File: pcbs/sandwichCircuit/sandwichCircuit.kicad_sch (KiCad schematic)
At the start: 1 part, among them U1 ESP32-DevKitC

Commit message: Progress sandwhich board
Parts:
- added IC1: 3678, 3678, symbol SamacSys_Parts:3678
- added J1: NodeMCU aux header, Connector_PinHeader_2.54mm:PinHeader_1x19_P2.54mm_Vertical, symbol Connector:Conn_01x19_Pin
- added J2: North Connector, Connector_PinSocket_2.54mm:PinSocket_1x06_P2.54mm_Vertical, symbol Connector_Generic:Conn_01x06
- added J3: East Connector, Connector_PinSocket_2.54mm:PinSocket_1x06_P2.54mm_Vertical, symbol Connector_Generic:Conn_01x06
- added J4: West Connector, Connector_PinSocket_2.54mm:PinSocket_1x06_P2.54mm_Vertical, symbol Connector_Generic:Conn_01x06
- added J5: Audio Out, Connector_PinHeader_2.54mm:PinHeader_1x03_P2.54mm_Vertical, symbol Connector_Generic:Conn_01x03
- U1: value ESP32-DevKitC -> ESP32-DevKitC header; footprint 113990105 -> Espressif:ESP32-DevKitC
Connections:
- net +3.3V: now reaches U1.1 (3V3)
- net +3.3V: now also IC1.2 (3VD), J2.5 (Pin_5)
- net BCLK: now reaches U1.10 (DAC_2/ADC2_CH9/GPIO26)
- net BCLK: now also IC1.6 (BCLK)
- net GND: now reaches U1.14 (GND), U1.32 (GND), U1.38 (GND)
- net GND: now also IC1.3 (GND), J1.1 (Pin_1), J1.7 (Pin_7), J2.1 (Pin_1)
- net +5V: now reaches U1.19 (5V)
- net +5V: now also IC1.1 (VIN), J2.4 (Pin_4)
- net CLK: now reaches U1.20 (SD_CLK/GPIO6)
- net CLK: now also J1.19 (Pin_19)
- net D0: now reaches U1.21 (SD_DATA0/GPIO7)
- net D0: now also J1.18 (Pin_18)
- net D1: now reaches U1.22 (SD_DATA1/GPIO8)
- net D1: now also J1.17 (Pin_17)
- net GPIO15: now reaches U1.23 (MTDO/GPIO15/ADC2_CH3)
- net GPIO15: now also J1.16 (Pin_16)
- net GPIO2: now reaches U1.24 (ADC2_CH2/GPIO2)
- net GPIO2: now also J1.15 (Pin_15)
- net GPIO0: now reaches U1.25 (GPIO0/BOOT/ADC2_CH1)
- net GPIO0: now also J1.14 (Pin_14)
- net GPIO4: now reaches U1.26 (ADC2_CH0/GPIO4)
- net GPIO4: now also J1.13 (Pin_13)
- net GPIO16/U1RXD: now reaches U1.27 (GPIO16)
- net GPIO16/U1RXD: now also J1.12 (Pin_12)
- net GPIO17/U1TXD: now reaches U1.28 (GPIO17)
- net GPIO17/U1TXD: now also J1.11 (Pin_11)
- net GPIO5: now reaches U1.29 (GPIO5)
- net GPIO5: now also J1.10 (Pin_10)
- net GPIO18: now reaches U1.30 (GPIO18)
- net GPIO18: now also J1.9 (Pin_9)
- net GPIO19: now reaches U1.31 (GPIO19)
- net GPIO19: now also J1.8 (Pin_8)
- net GPIO21: now reaches U1.33 (GPIO21)
- net GPIO21: now also J1.6 (Pin_6)
- net GPIO3/U0RXD: now reaches U1.34 (U0RXD/GPIO3)
- net GPIO3/U0RXD: now also J1.5 (Pin_5)
- net GPIO1/U0TXD: now reaches U1.35 (U0TXD/GPIO1)
- net GPIO1/U0TXD: now also J1.4 (Pin_4)
- net DIN: now reaches U1.36 (GPIO22)
- net DIN: now also IC1.5 (DIN), J1.3 (Pin_3)
- net GPIO23: now reaches U1.37 (GPIO23)
- net GPIO23: now also J1.2 (Pin_2)
- net WSEL: now reaches U1.9 (DAC_1/ADC2_CH8/GPIO25)
- net WSEL: now also IC1.4 (WSEL)
- new net AGND: IC1.8 (AGND), J5.1 (Pin_1)
- new net CTS: J4.2 (Pin_2)
- new net DCD: J4.5 (Pin_5)
- new net DSR: J4.4 (Pin_4)
- new net DTR: J2.6 (Pin_6)
- new net IO0: J3.5 (Pin_5)
- new net IO1: J3.4 (Pin_4)
- new net IO2: J3.3 (Pin_3)
- new net IO3: J3.2 (Pin_2)
- new net LOUT: IC1.7 (LOUT), J5.3 (Pin_3)
- new net RI: J4.6 (Pin_6)
- new net ROUT: IC1.9 (ROUT), J5.2 (Pin_2)
- new net RST: J3.1 (Pin_1)
- new net RTS: J4.3 (Pin_3)
- new net RXD: J2.2 (Pin_2)
- new net SPD: J4.1 (Pin_1)
- new net SPD-: J3.6 (Pin_6)
- new net TXD: J2.3 (Pin_3)
- no-connect marks 0 -> 24

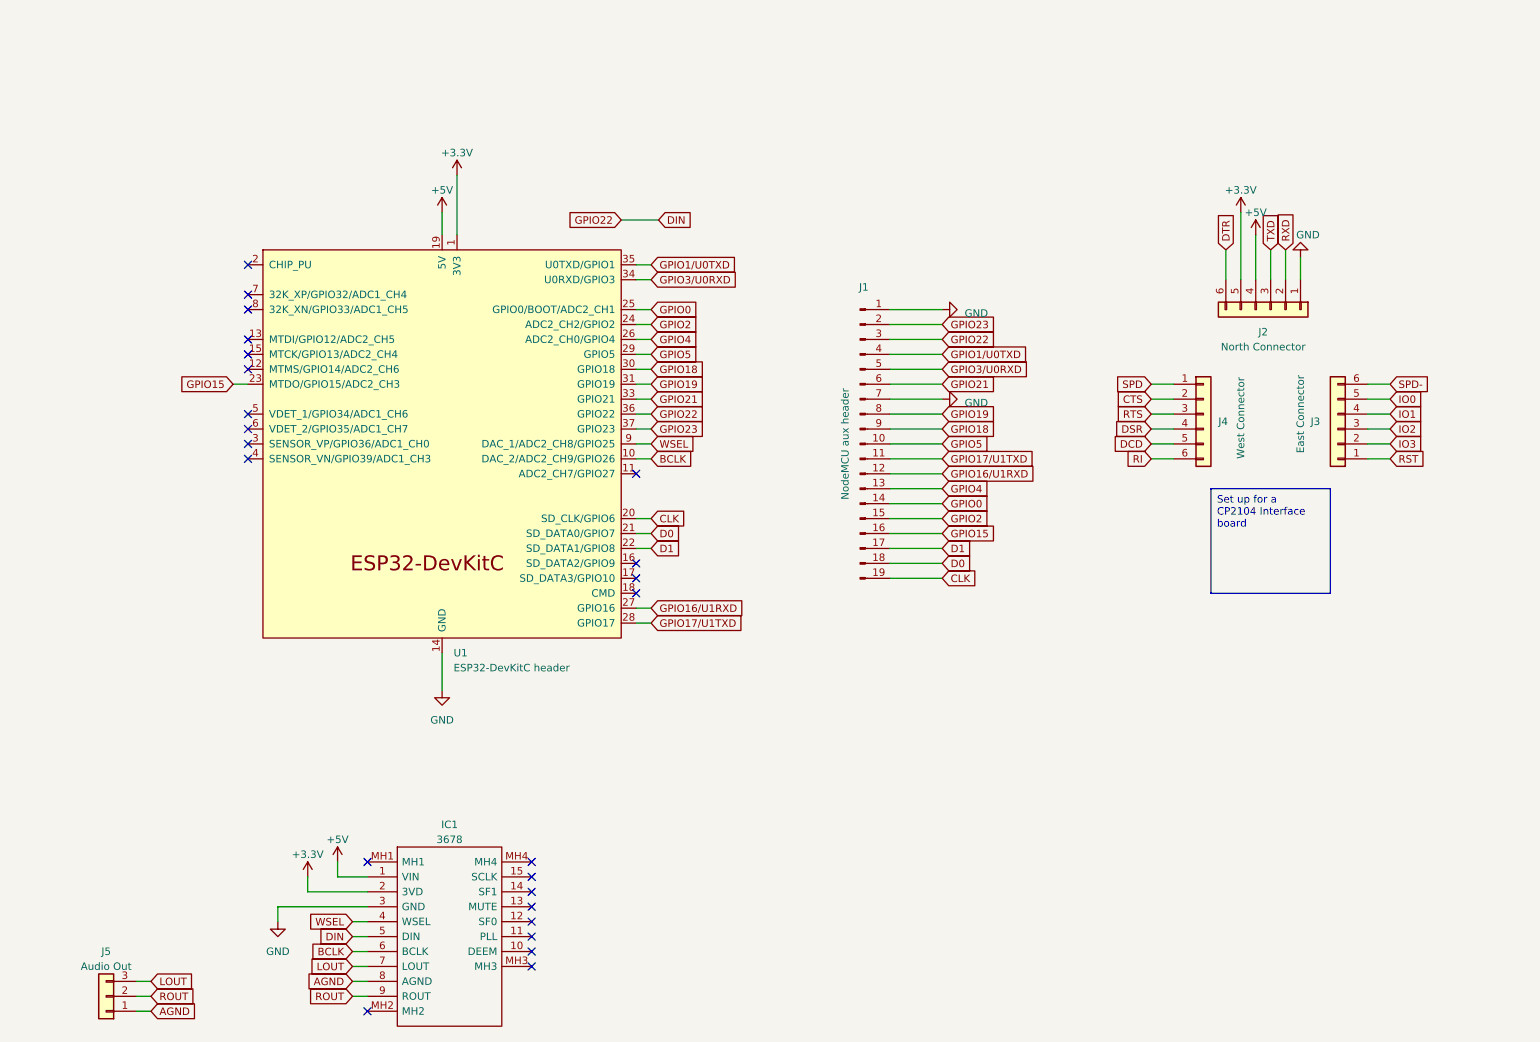
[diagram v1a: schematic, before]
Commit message: Simplified footprints, schematic revisited
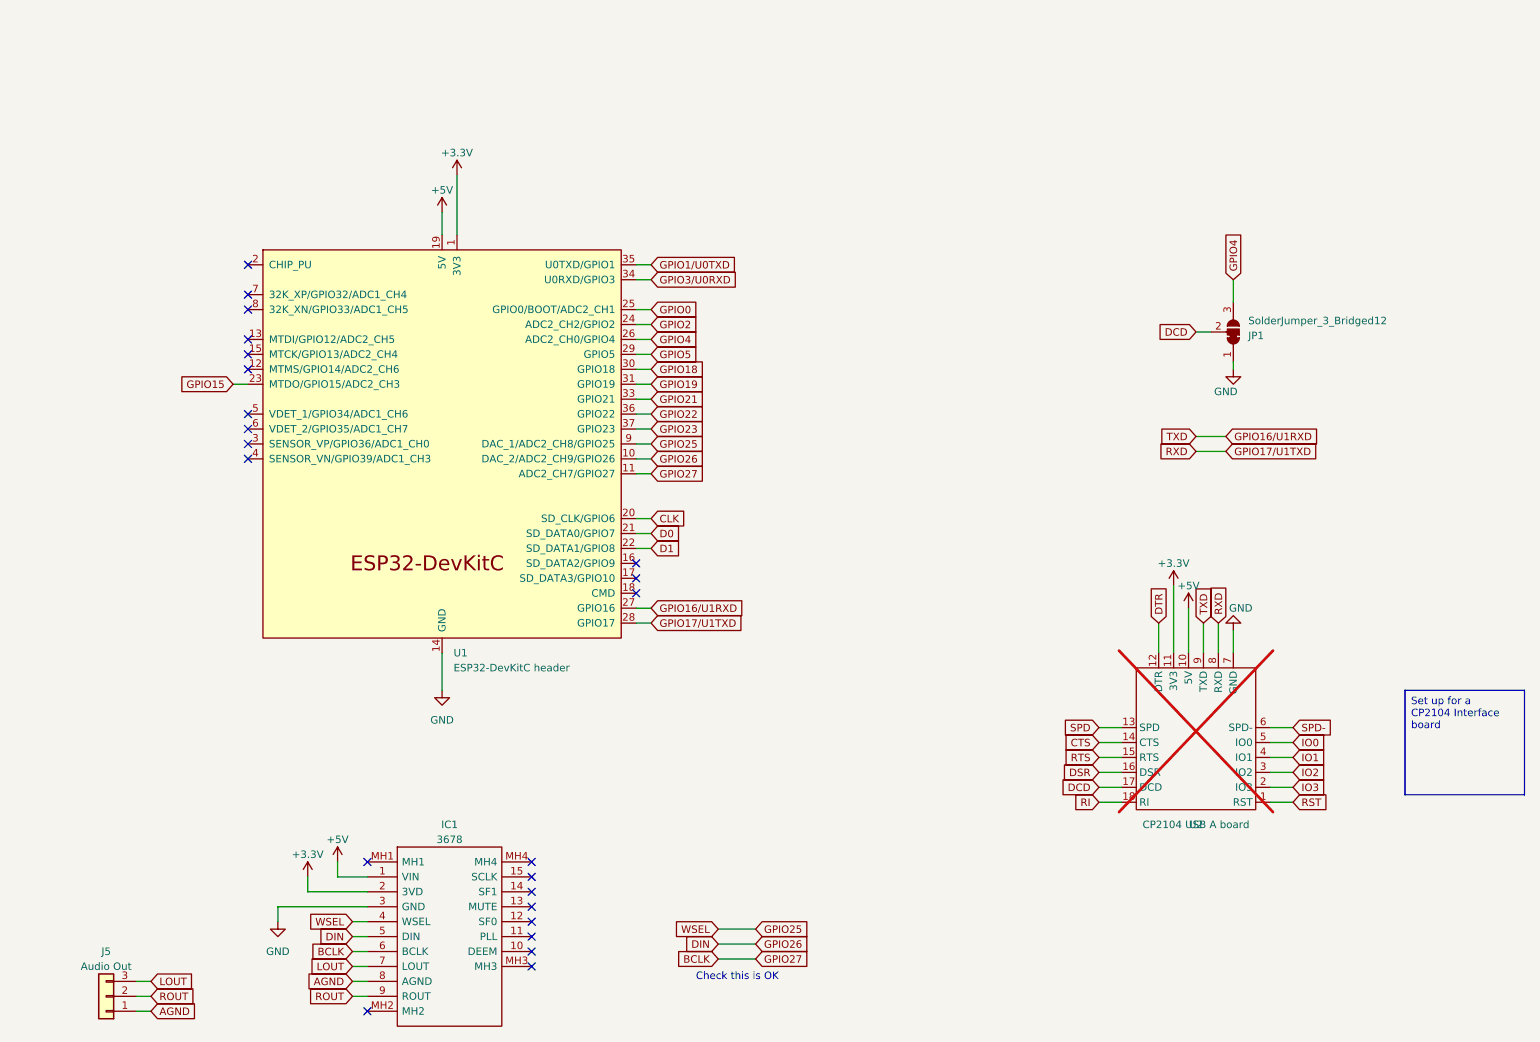
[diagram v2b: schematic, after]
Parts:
- removed J1: NodeMCU aux header, Connector_PinHeader_2.54mm:PinHeader_1x19_P2.54mm_Vertical, symbol Connector:Conn_01x19_Pin
- removed J2: North Connector, Connector_PinSocket_2.54mm:PinSocket_1x06_P2.54mm_Vertical, symbol Connector_Generic:Conn_01x06
- removed J3: East Connector, Connector_PinSocket_2.54mm:PinSocket_1x06_P2.54mm_Vertical, symbol Connector_Generic:Conn_01x06
- removed J4: West Connector, Connector_PinSocket_2.54mm:PinSocket_1x06_P2.54mm_Vertical, symbol Connector_Generic:Conn_01x06
- added JP1: SolderJumper_3_Bridged12, Jumper:SolderJumper-3_P1.3mm_Bridged12_RoundedPad1.0x1.5mm, symbol Jumper:SolderJumper_3_Bridged12
- added U2: CP2104 USB A board, DIY:CP2104_USB_Board, symbol DIY:CP2104_UART_Board
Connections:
- net +3.3V: now also U2.11 (3V3)
- net +5V: now also U2.10 (5V)
- net BCLK: now also U1.11 (ADC2_CH7/GPIO27); no longer U1.10 (DAC_2/ADC2_CH9/GPIO26)
- net CTS: now also U2.14 (CTS)
- net DCD: now also JP1.2 (C), U2.17 (DCD)
- net DIN: now also U1.10 (DAC_2/ADC2_CH9/GPIO26); no longer U1.36 (GPIO22)
- net DSR: now also U2.16 (DSR)
- net DTR: now also U2.12 (DTR)
- net GND: now also JP1.1 (A), U2.7 (GND)
- net GPIO16/U1RXD: now also U2.9 (TXD)
- net GPIO17/U1TXD: now also U2.8 (RXD)
- net GPIO4: now also JP1.3 (B)
- net IO0: now also U2.5 (IO0)
- net IO1: now also U2.4 (IO1)
- net IO2: now also U2.3 (IO2)
- net IO3: now also U2.2 (IO3)
- net RI: now also U2.18 (RI)
- net RST: now also U2.1 (RST)
- net RTS: now also U2.15 (RTS)
- net SPD: now also U2.13 (SPD)
- net SPD-: now also U2.6 (SPD-)
- net WSEL renamed GPIO25
- new net GPIO22: U1.36 (GPIO22)
- no-connect marks 24 -> 23
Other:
- note added: "Check this is OK"

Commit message: v0.1 of simple carrier board
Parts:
- added H1, H2, H3, H4: MountingHole_Pad, MountingHole:MountingHole_3.2mm_M3_Pad_TopBottom, symbol Mechanical:MountingHole_Pad
- IC1: footprint 3678 -> DIY:Adafruit 3678
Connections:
- net AGND: now also J5.2 (Pin_2); no longer J5.1 (Pin_1)
- net GND: now also H1.1, H2.1, H3.1, H4.1
- net ROUT: now also J5.1 (Pin_1); no longer J5.2 (Pin_2)
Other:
- title: (none) -> Simple carrier board (CP2104)
- moved on the sheet: J5, JP1

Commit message: Sandwich board 0.1.1
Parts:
- added JP2: SolderJumper_2_Bridged, Jumper:SolderJumper-2_P1.3mm_Bridged_RoundedPad1.0x1.5mm, symbol Jumper:SolderJumper_2_Bridged
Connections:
- net GND: now also JP2.2 (B)
- net GPIO15: now also JP2.1 (A)
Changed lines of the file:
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@@
   (title_block
     (title "Simple carrier board (CP2104)")
-    (date "2025-02-20")
-    (rev "0.1")
+    (date "2025-02-26")
+    (rev "0.1.1")
   )
   (junction (at 85.09 50.8) (diameter 0) (color 0 0 0 0)
@@
     (stroke (width 0) (type default))
   )
+  (wire (pts (xy 64.77 140.97) (xy 69.85 140.97))
+    (stroke (width 0) (type default))
+  )
   (wire (pts (xy 163.83 52.07) (xy 182.88 52.07))
     (stroke (width 0) (type default))
@@
     (stroke (width 0) (type default))
   )
+  (wire (pts (xy 48.26 140.97) (xy 57.15 140.97))
+    (stroke (width 0) (type default))
+  )
   (wire (pts (xy 69.85 177.8) (xy 72.39 177.8))
     (stroke (width 0) (type default))
@@
   )
   (wire (pts (xy 87.63 50.8) (xy 93.98 50.8))
+    (stroke (width 0) (type default))
+  )
+  (wire (pts (xy 69.85 140.97) (xy 69.85 143.51))
     (stroke (width 0) (type default))
   )
@@
     (property "Intersheetrefs" "${INTERSHEET_REFS}" (at 135.904 58.42 0)
       (effects (font (size 1.27 1.27)) (justify left) hide)
+    )
+  )
+  (global_label "GPIO15" (shape input) (at 48.26 140.97 180) (fields_autoplaced)
+    (effects (font (size 1.27 1.27)) (justify right))
+    (property "Intersheetrefs" "${INTERSHEET_REFS}" (at 39.1141 140.97 0)
+      (effects (font (size 1.27 1.27)) (justify right) hide)
     )
   )
@@
     )
   )
+  (symbol (lib_id "Jumper:SolderJumper_2_Bridged") (at 60.96 140.97 0) (unit 1)
+    (in_bom yes) (on_board yes) (dnp no) (fields_autoplaced)
+    (property "Reference" "JP2" (at 60.96 135.89 0)
+      (effects (font (size 1.27 1.27)))
+    )
+    (property "Value" "SolderJumper_2_Bridged" (at 60.96 138.43 0)
+      (effects (font (size 1.27 1.27)))
+    )
+    (property "Footprint" "Jumper:SolderJumper-2_P1.3mm_Bridged_RoundedPad1.0x1.5mm" (at 60.96 140.97 0)
+      (effects (font (size 1.27 1.27)) hide)
+    )
+    (property "Datasheet" "~" (at 60.96 140.97 0)
+      (effects (font (size 1.27 1.27)) hide)
+    )
+    (pin "1")
+    (pin "2")
+    (instances
+      (project "sandwichCircuit"
+        (path "/473bba75-08f8-4c6c-a9b2-aa3e95e63a5e"
+          (reference "JP2") (unit 1)
+        )
+      )
+    )
+  )
   (symbol (lib_id "Mechanical:MountingHole_Pad") (at 154.94 144.78 0) (unit 1)
     (in_bom yes) (on_board yes) (dnp no) (fields_autoplaced)
@@
         )
       )
+    )
+  )
+  (symbol (lib_id "power:GND") (at 69.85 143.51 0) (unit 1)
+    (in_bom yes) (on_board yes) (dnp no) (fields_autoplaced)
+    (property "Reference" "#PWR015" (at 69.85 149.86 0)
+      (effects (font (size 1.27 1.27)) hide)
+    )
+    (property "Value" "GND" (at 69.85 148.59 0)
+      (effects (font (size 1.27 1.27)))
+    )
+    (property "Footprint" "" (at 69.85 143.51 0)
+      (effects (font (size 1.27 1.27)) hide)
+    )
+    (property "Datasheet" "" (at 69.85 143.51 0)
+      (effects (font (size 1.27 1.27)) hide)
+    )
+    (pin "1")
+    (instances
+      (project "sandwichCircuit"
+        (path "/473bba75-08f8-4c6c-a9b2-aa3e95e63a5e"
+          (reference "#PWR015") (unit 1)
+        )
+      )

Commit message: Sandwich board adjustments
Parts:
- IC1, U1: now not fitted; now left out of the parts list
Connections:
- net GPIO4: no longer JP1.3 (B)
- net GPIO5: now also JP1.3 (B)
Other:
- company: (none) -> Martin Roger
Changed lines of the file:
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@@
   (title_block
     (title "Simple carrier board (CP2104)")
-    (date "2025-02-26")
-    (rev "0.1.1")
+    (date "2025-03-01")
+    (rev "0.1.3")
+    (company "Martin Roger")
   )
   (junction (at 85.09 50.8) (diameter 0) (color 0 0 0 0)
@@
     )
   )
+  (global_label "GPIO5" (shape input) (at 184.15 25.4 90) (fields_autoplaced)
+    (effects (font (size 1.27 1.27)) (justify left))
+    (property "Intersheetrefs" "${INTERSHEET_REFS}" (at 184.15 17.4636 90)
+      (effects (font (size 1.27 1.27)) (justify left) hide)
+    )
+  )
   (global_label "LOUT" (shape input) (at 25.4 180.34 0) (fields_autoplaced)
     (effects (font (size 1.27 1.27)) (justify left))
     (property "Intersheetrefs" "${INTERSHEET_REFS}" (at 32.3083 180.34 0)
-      (effects (font (size 1.27 1.27)) (justify left) hide)
-    )
-  )
-  (global_label "GPIO4" (shape input) (at 184.15 25.4 90) (fields_autoplaced)
-    (effects (font (size 1.27 1.27)) (justify left))
-    (property "Intersheetrefs" "${INTERSHEET_REFS}" (at 184.15 17.4636 90)
       (effects (font (size 1.27 1.27)) (justify left) hide)
     )
@@
   )
   (symbol (lib_id "Espressif:ESP32-DevKitC") (at 85.09 88.9 0) (unit 1)
-    (in_bom yes) (on_board yes) (dnp no) (fields_autoplaced)
+    (in_bom no) (on_board yes) (dnp yes) (fields_autoplaced)
     (property "Reference" "U1" (at 87.0459 124.46 0)
       (effects (font (size 1.27 1.27)) (justify left))
@@
   )
   (symbol (lib_id "SamacSys_Parts:3678") (at 72.39 160.02 0) (unit 1)
-    (in_bom yes) (on_board yes) (dnp no) (fields_autoplaced)
+    (in_bom no) (on_board yes) (dnp yes) (fields_autoplaced)
     (property "Reference" "IC1" (at 86.36 153.67 0)
       (effects (font (size 1.27 1.27)))

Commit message: Projects consistency update
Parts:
- IC1: footprint DIY:Adafruit 3678 -> DIY:3678; symbol SamacSys_Parts:3678 -> DIY:3678; now in the parts list
- U1: footprint Espressif:ESP32-DevKitC -> PCM_Espressif:ESP32-DevKitC; symbol Espressif:ESP32-DevKitC -> PCM_Espressif:ESP32-DevKitC; now in the parts list

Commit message: Update SCB
Updated SCB :
- Upper pins of CP2104 moved about 0.5mm up
- CP2104 reset is now available on GPIO 13
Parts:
- added JP3: SolderJumper_2_Open, Jumper:SolderJumper-2_P1.3mm_Open_RoundedPad1.0x1.5mm, symbol Jumper:SolderJumper_2_Open
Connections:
- net RST: now also JP3.2 (B)
- net GPIO13: now reaches U1.15 (MTCK/GPIO13/ADC2_CH4)
- net GPIO13: now also JP3.1 (A)
- no-connect marks 23 -> 22

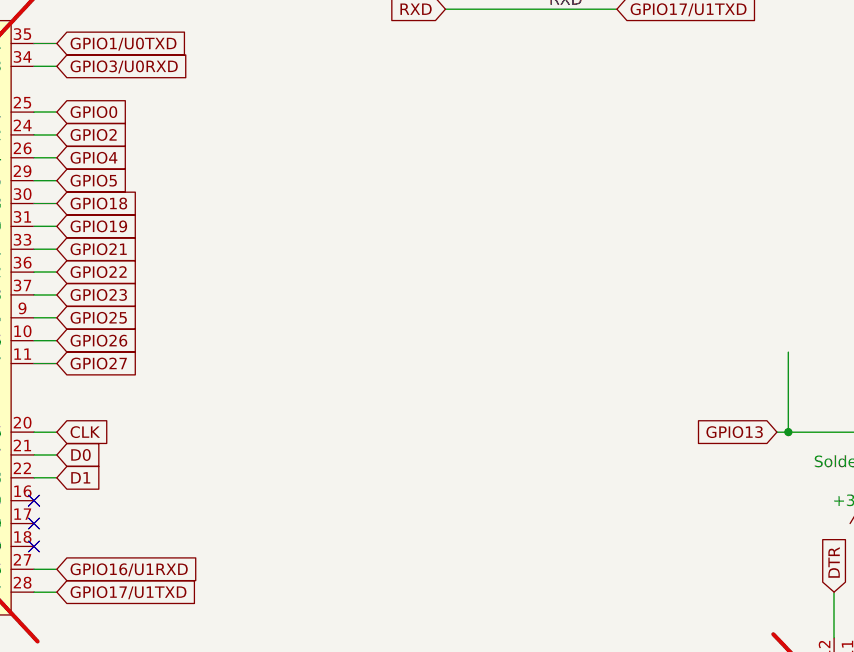
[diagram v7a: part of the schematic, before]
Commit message: Adding bulk 5V capacitor to SCB
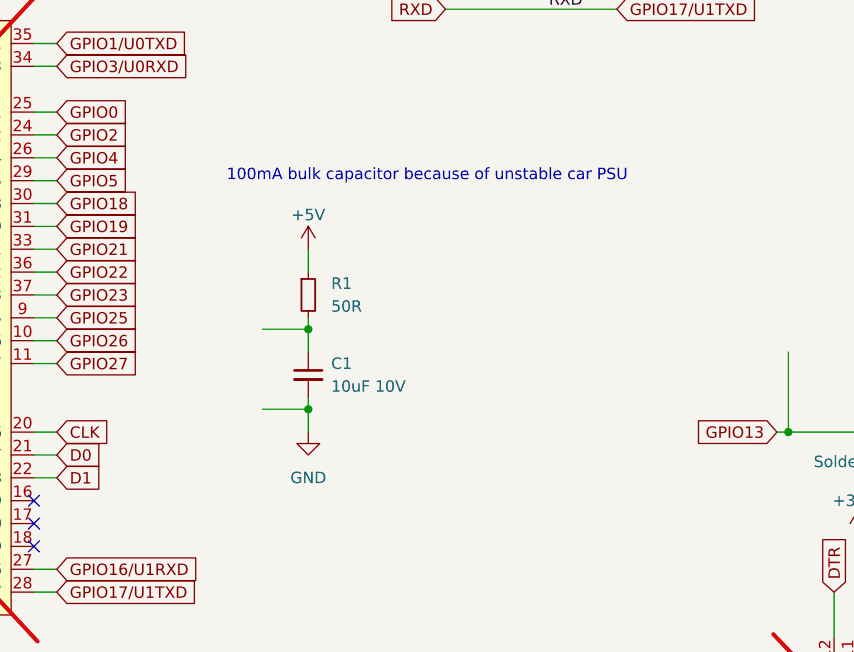
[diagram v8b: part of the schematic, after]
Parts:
- added C1: 10uF 10V, Capacitor_THT:C_Radial_D5.0mm_H7.0mm_P2.00mm, symbol Device:C_Small
- added R1: 50R, Resistor_THT:R_Axial_DIN0207_L6.3mm_D2.5mm_P10.16mm_Horizontal, symbol Device:R_Small
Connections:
- net +5V: now also R1.1
- net GND: now also C1.2
- new net: C1.1, R1.2
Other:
- note added: "100mA bulk capacitor because of unstable car PSU"
